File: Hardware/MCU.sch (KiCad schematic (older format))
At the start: 8 parts, among them J2 LCD_and_RotEnc, U10 74HC14, U9 BluePill_STM32F103C

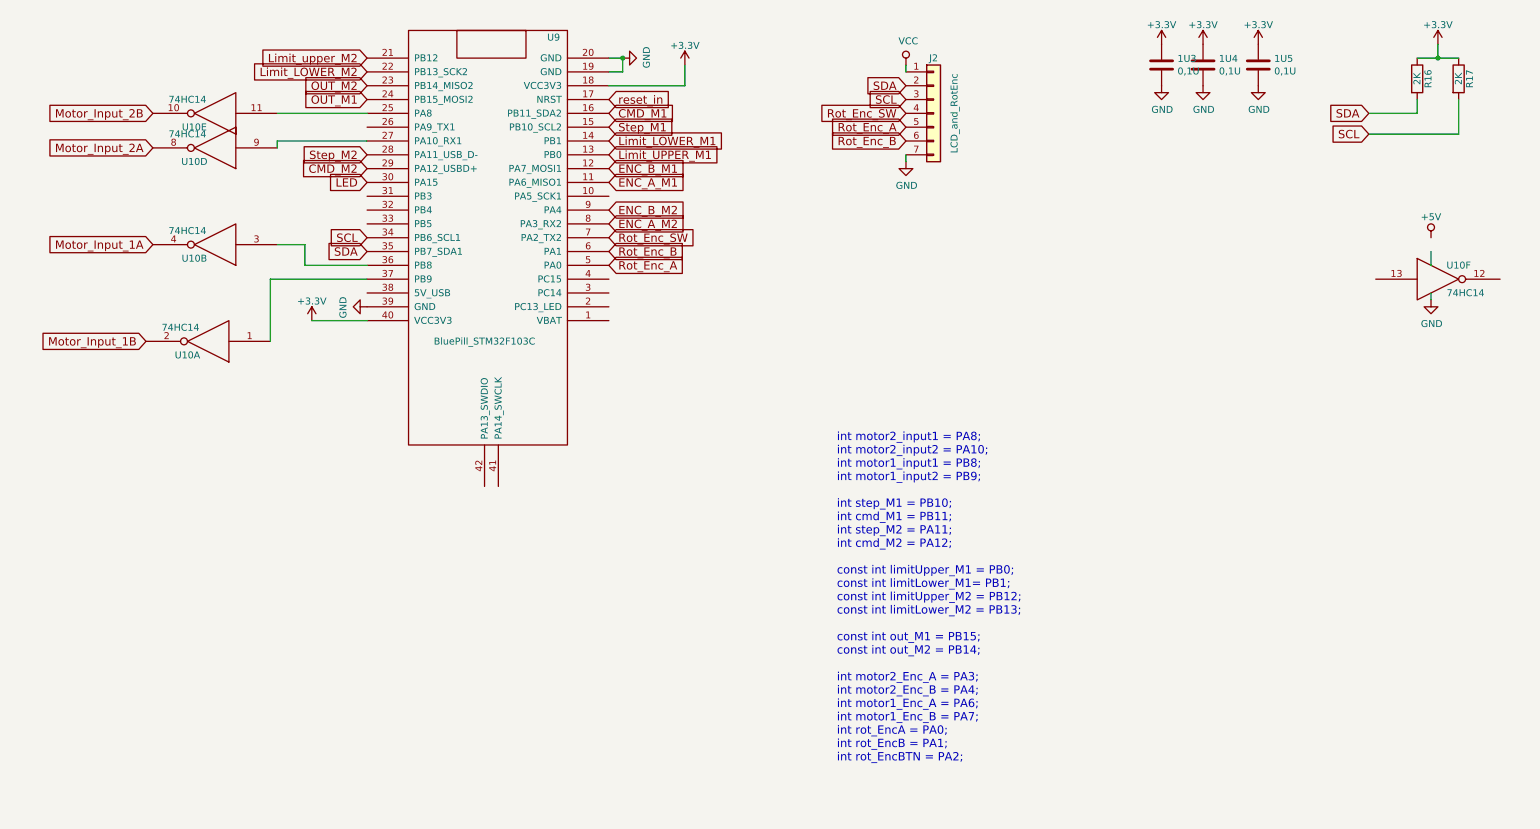
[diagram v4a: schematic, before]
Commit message: one motor
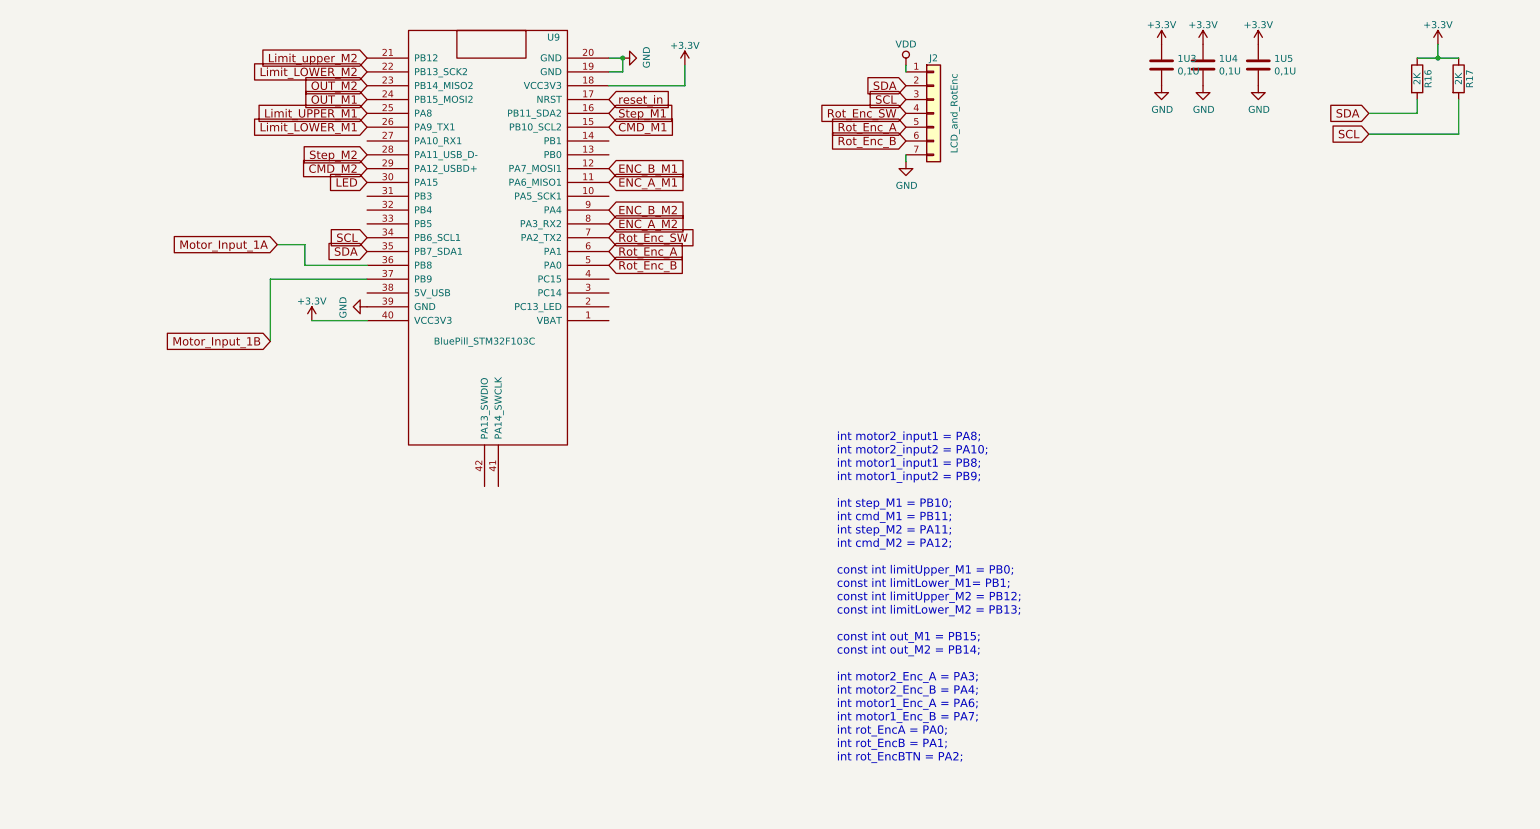
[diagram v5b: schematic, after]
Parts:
- removed U10: 74HC14, Housings_SOIC:SOIC-14_3.9x8.7mm_Pitch1.27mm, symbol 74HC14
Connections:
- net labels added: VDD
- net labels removed: +5V, Motor_Input_2A, Motor_Input_2B, VCC
- wire segments 24 -> 19
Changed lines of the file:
@@
 $EndComp
 $Comp
-L GND #PWR030
+L GND #PWR021
 U 1 1 5A674C98
 P 8550 1200
-F 0 "#PWR030" H 8550 950 50  0001 C CNN
+F 0 "#PWR021" H 8550 950 50  0001 C CNN
 F 1 "GND" H 8555 1027 50  0000 C CNN
 F 2 "" H 8550 1200 50  0001 C CNN
@@
 $EndComp
 $Comp
-L GND #PWR031
+L GND #PWR022
 U 1 1 5A674CAB
 P 9250 1200
-F 0 "#PWR031" H 9250 950 50  0001 C CNN
+F 0 "#PWR022" H 9250 950 50  0001 C CNN
 F 1 "GND" H 9255 1027 50  0000 C CNN
 F 2 "" H 9250 1200 50  0001 C CNN
@@
 Text GLabel 2800 1300 0    60   Input ~ 0
 OUT_M1
-Text GLabel 4550 1500 2    60   Input ~ 0
+Text GLabel 4550 1400 2    60   Input ~ 0
 Step_M1
 Text GLabel 2800 1800 0    60   Input ~ 0
@@
 $EndComp
 $Comp
-L GND #PWR032
+L GND #PWR023
 U 1 1 5A674CDA
 P 8850 1200
-F 0 "#PWR032" H 8850 950 50  0001 C CNN
+F 0 "#PWR023" H 8850 950 50  0001 C CNN
 F 1 "GND" H 8855 1027 50  0000 C CNN
 F 2 "" H 8850 1200 50  0001 C CNN
@@
 Text GLabel 2800 2300 0    60   Input ~ 0
 SCL
-Text GLabel 1250 2350 0    60   Input ~ 0
+Text GLabel 2150 2350 0    60   Input ~ 0
 Motor_Input_1A
-Text GLabel 1200 3050 0    60   Input ~ 0
+Text GLabel 2100 3050 0    60   Input ~ 0
 Motor_Input_1B
-Text GLabel 1250 1650 0    60   Input ~ 0
-Motor_Input_2A
-Text GLabel 1250 1400 0    60   Input ~ 0
-Motor_Input_2B
-Text GLabel 4550 1600 2    60   Input ~ 0
+Text GLabel 2800 1500 0    60   Input ~ 0
 Limit_LOWER_M1
 Text GLabel 2800 1000 0    60   Input ~ 0
 Limit_upper_M2
-Text GLabel 4550 1700 2    60   Input ~ 0
+Text GLabel 2800 1400 0    60   Input ~ 0
 Limit_UPPER_M1
 Text GLabel 2800 1100 0    60   Input ~ 0
@@
 Text GLabel 4550 2300 2    60   Input ~ 0
 Rot_Enc_SW
+Text GLabel 4550 2500 2    60   Input ~ 0
+Rot_Enc_B
 Text GLabel 4550 2400 2    60   Input ~ 0
-Rot_Enc_B
-Text GLabel 4550 2500 2    60   Input ~ 0
 Rot_Enc_A
-Text GLabel 4550 1400 2    60   Input ~ 0
+Text GLabel 4550 1500 2    60   Input ~ 0
 CMD_M1
 Text GLabel 2800 1700 0    60   Input ~ 0
@@
 $EndComp
 $Comp
-L GND #PWR033
+L GND #PWR024
 U 1 1 5A679D8E
 P 4650 1000
-F 0 "#PWR033" H 4650 750 50  0001 C CNN
+F 0 "#PWR024" H 4650 750 50  0001 C CNN
 F 1 "GND" H 4655 827 50  0000 C CNN
 F 2 "" H 4650 1000 50  0001 C CNN
@@
 Connection ~ 4650 1000
 $Comp
-L GND #PWR034
+L GND #PWR025
 U 1 1 5A679DFB
 P 2800 2800
-F 0 "#PWR034" H 2800 2550 50  0001 C CNN
+F 0 "#PWR025" H 2800 2550 50  0001 C CNN
 F 1 "GND" H 2805 2627 50  0000 C CNN
 F 2 "" H 2800 2800 50  0001 C CNN
@@
 Wire Wire Line
 	4550 1200 5100 1200
-$Comp
-L 74HC14 U10
-U 1 1 5A67D171
-P 1650 3050
-F 0 "U10" H 1800 3150 50  0000 C CNN
-F 1 "74HC14" H 1850 2950 50  0000 C CNN
-F 2 "Housings_SOIC:SOIC-14_3.9x8.7mm_Pitch1.27mm" H 1650 3050 50  0001 C CNN
-F 3 "" H 1650 3050 50  0001 C CNN
-	1    1650 3050
-	-1   0    0    1
-$EndComp
-$Comp
-L 74HC14 U10
-U 2 1 5A67D1B2
-P 1700 2350
-F 0 "U10" H 1850 2450 50  0000 C CNN
-F 1 "74HC14" H 1900 2250 50  0000 C CNN
-F 2 "Housings_SOIC:SOIC-14_3.9x8.7mm_Pitch1.27mm" H 1700 2350 50  0001 C CNN
-F 3 "" H 1700 2350 50  0001 C CNN
-	2    1700 2350
-	-1   0    0    1
-$EndComp
-$Comp
-L 74HC14 U10
-U 5 1 5A67D1FD
-P 1700 1400
-F 0 "U10" H 1850 1500 50  0000 C CNN
-F 1 "74HC14" H 1900 1300 50  0000 C CNN
-F 2 "Housings_SOIC:SOIC-14_3.9x8.7mm_Pitch1.27mm" H 1700 1400 50  0001 C CNN
-F 3 "" H 1700 1400 50  0001 C CNN
-	5    1700 1400
-	-1   0    0    1
-$EndComp
-$Comp
-L 74HC14 U10
-U 4 1 5A67D24A
-P 1700 1650
-F 0 "U10" H 1850 1750 50  0000 C CNN
-F 1 "74HC14" H 1900 1550 50  0000 C CNN
-F 2 "Housings_SOIC:SOIC-14_3.9x8.7mm_Pitch1.27mm" H 1700 1650 50  0001 C CNN
-F 3 "" H 1700 1650 50  0001 C CNN
-	4    1700 1650
-	-1   0    0    1
-$EndComp
 Text GLabel 2800 1200 0    60   Input ~ 0
 OUT_M2
@@
 $EndComp
 $Comp
-L +3.3V #PWR035
+L +3.3V #PWR026
 U 1 1 5A68CA96
 P 10550 900
-F 0 "#PWR035" H 10550 750 50  0001 C CNN
+F 0 "#PWR026" H 10550 750 50  0001 C CNN
 F 1 "+3.3V" H 10550 1040 50  0000 C CNN
 F 2 "" H 10550 900 50  0001 C CNN
@@
 	10700 1550 10700 1300
 $Comp
-L VCC #PWR036
-U 1 1 5A707439
-P 6700 1050
-F 0 "#PWR036" H 6700 900 50  0001 C CNN
-F 1 "VCC" H 6717 1223 50  0000 C CNN
-F 2 "" H 6700 1050 50  0001 C CNN
-F 3 "" H 6700 1050 50  0001 C CNN
-	1    6700 1050
-	1    0    0    -1
-$EndComp
-$Comp
-L GND #PWR037
+L GND #PWR027
 U 1 1 5A70743F
 P 6700 1750
-F 0 "#PWR037" H 6700 1500 50  0001 C CNN
+F 0 "#PWR027" H 6700 1500 50  0001 C CNN
 F 1 "GND" H 6705 1577 50  0000 C CNN
 F 2 "" H 6700 1750 50  0001 C CNN
@@
 	2800 2900 2400 2900
 $Comp
-L +3.3V #PWR038
+L +3.3V #PWR028
 U 1 1 5A7153CF
 P 2400 2900
-F 0 "#PWR038" H 2400 2750 50  0001 C CNN
+F 0 "#PWR028" H 2400 2750 50  0001 C CNN
 F 1 "+3.3V" H 2400 3040 50  0000 C CNN
 F 2 "" H 2400 2900 50  0001 C CNN
@@
 $EndComp
 $Comp
-L +3.3V #PWR039
+L +3.3V #PWR029
 U 1 1 5A715491
 P 8850 900
-F 0 "#PWR039" H 8850 750 50  0001 C CNN
+F 0 "#PWR029" H 8850 750 50  0001 C CNN
 F 1 "+3.3V" H 8850 1040 50  0000 C CNN
 F 2 "" H 8850 900 50  0001 C CNN
@@
 $EndComp
 $Comp
-L +3.3V #PWR040
+L +3.3V #PWR030
 U 1 1 5A7154F3
 P 8550 900
-F 0 "#PWR040" H 8550 750 50  0001 C CNN
+F 0 "#PWR030" H 8550 750 50  0001 C CNN
 F 1 "+3.3V" H 8550 1040 50  0000 C CNN
 F 2 "" H 8550 900 50  0001 C CNN
@@
 $EndComp
 $Comp
-L +3.3V #PWR041
+L +3.3V #PWR031
 U 1 1 5A715555
 P 9250 900
-F 0 "#PWR041" H 9250 750 50  0001 C CNN
+F 0 "#PWR031" H 9250 750 50  0001 C CNN
 F 1 "+3.3V" H 9250 1040 50  0000 C CNN
 F 2 "" H 9250 900 50  0001 C CNN
@@
 $EndComp
 $Comp
-L +3.3V #PWR042
+L +3.3V #PWR032
 U 1 1 5A71590E
 P 5100 1050
-F 0 "#PWR042" H 5100 900 50  0001 C CNN
+F 0 "#PWR032" H 5100 900 50  0001 C CNN
 F 1 "+3.3V" H 5100 1190 50  0000 C CNN
 F 2 "" H 5100 1050 50  0001 C CNN
@@
 	1    0    0    -1
 $EndComp
-$Comp
-L 74HC14 U10
-U 6 1 5A715D65
-P 10550 2600
-F 0 "U10" H 10700 2700 50  0000 C CNN
-F 1 "74HC14" H 10750 2500 50  0000 C CNN
-F 2 "Housings_SOIC:SOIC-14_3.9x8.7mm_Pitch1.27mm" H 10550 2600 50  0001 C CNN
-F 3 "" H 10550 2600 50  0001 C CNN
-	6    10550 2600
-	1    0    0    -1
-$EndComp
-Wire Wire Line
-	10500 2400 10500 2500
-$Comp
-L GND #PWR043
-U 1 1 5A7162E9
-P 10500 2750
-F 0 "#PWR043" H 10500 2500 50  0001 C CNN
-F 1 "GND" H 10505 2577 50  0000 C CNN
-F 2 "" H 10500 2750 50  0001 C CNN
-F 3 "" H 10500 2750 50  0001 C CNN
-	1    10500 2750
-	1    0    0    -1
-$EndComp
-Wire Wire Line
-	10500 2700 10500 2750
 Text Notes 6200 6100 0    60   ~ 0
 int motor2_input1 = PA8;\nint motor2_input2 = PA10;\nint motor1_input1 = PB8;\nint motor1_input2 = PB9;\n\nint step_M1 = PB10;\nint cmd_M1 = PB11;\nint step_M2 = PA11;\nint cmd_M2 = PA12;\n\nconst int limitUpper_M1 = PB0;\nconst int limitLower_M1= PB1;\nconst int limitUpper_M2 = PB12;\nconst int limitLower_M2 = PB13;\n\nconst int out_M1 = PB15;\nconst int out_M2 = PB14;\n\nint motor2_Enc_A = PA3;\nint motor2_Enc_B = PA4;\nint motor1_Enc_A = PA6;\nint motor1_Enc_B = PA7;\nint rot_EncA = PA0;\nint rot_EncB = PA1;\nint rot_EncBTN = PA2;\n
 Wire Wire Line
-	2150 1400 2800 1400
-Wire Wire Line
-	2800 1600 2150 1600
-Wire Wire Line
-	2150 1600 2150 1650
-Wire Wire Line
 	2350 2500 2800 2500
 Wire Wire Line
@@
 Wire Wire Line
 	2100 2600 2800 2600
-$Comp
-L VDD #PWR044
-U 1 1 5A7C31A2
-P 10500 2300
-F 0 "#PWR044" H 10500 2150 50  0001 C CNN
-F 1 "+5V" H 10500 2450 50  0000 C CNN
-F 2 "" H 10500 2300 50  0001 C CNN
-F 3 "" H 10500 2300 50  0001 C CNN
-	1    10500 2300
-	1    0    0    -1
-$EndComp
 Text GLabel 2800 1900 0    60   Input ~ 0
 LED
@@
 Wire Wire Line
 	6700 1050 6700 1100
+$Comp
+L VDD #PWR033
+U 1 1 5AAFC557
+P 6700 1050
+F 0 "#PWR033" H 6700 900 50  0001 C CNN
+F 1 "VDD" H 6700 1200 50  0000 C CNN
+F 2 "" H 6700 1050 50  0001 C CNN
+F 3 "" H 6700 1050 50  0001 C CNN
+	1    6700 1050
+	1    0    0    -1
+$EndComp
 $EndSCHEMATC
